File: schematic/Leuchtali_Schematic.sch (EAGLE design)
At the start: 34 parts, among them IC1 LM1458D, IC2 LM1458D, IC3 LM1458D, IC4 LT1618EMS#PBF

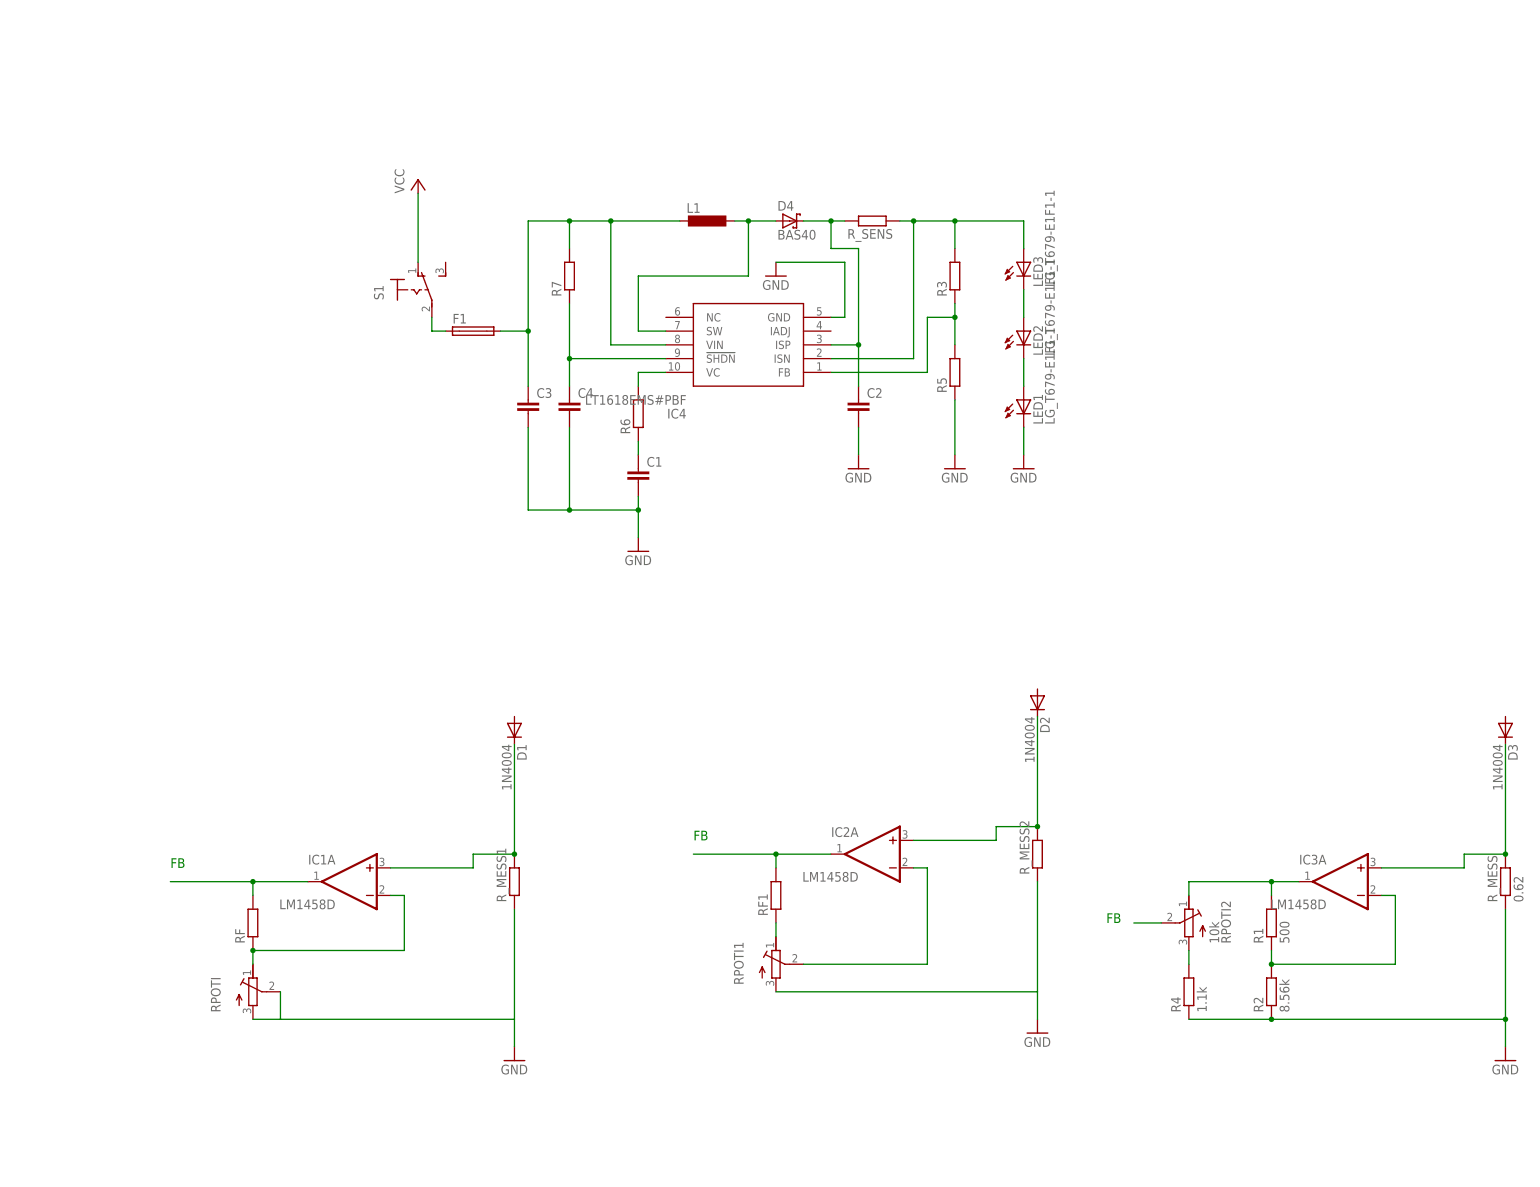
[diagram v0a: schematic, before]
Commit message: Removed old ideas from the schematic
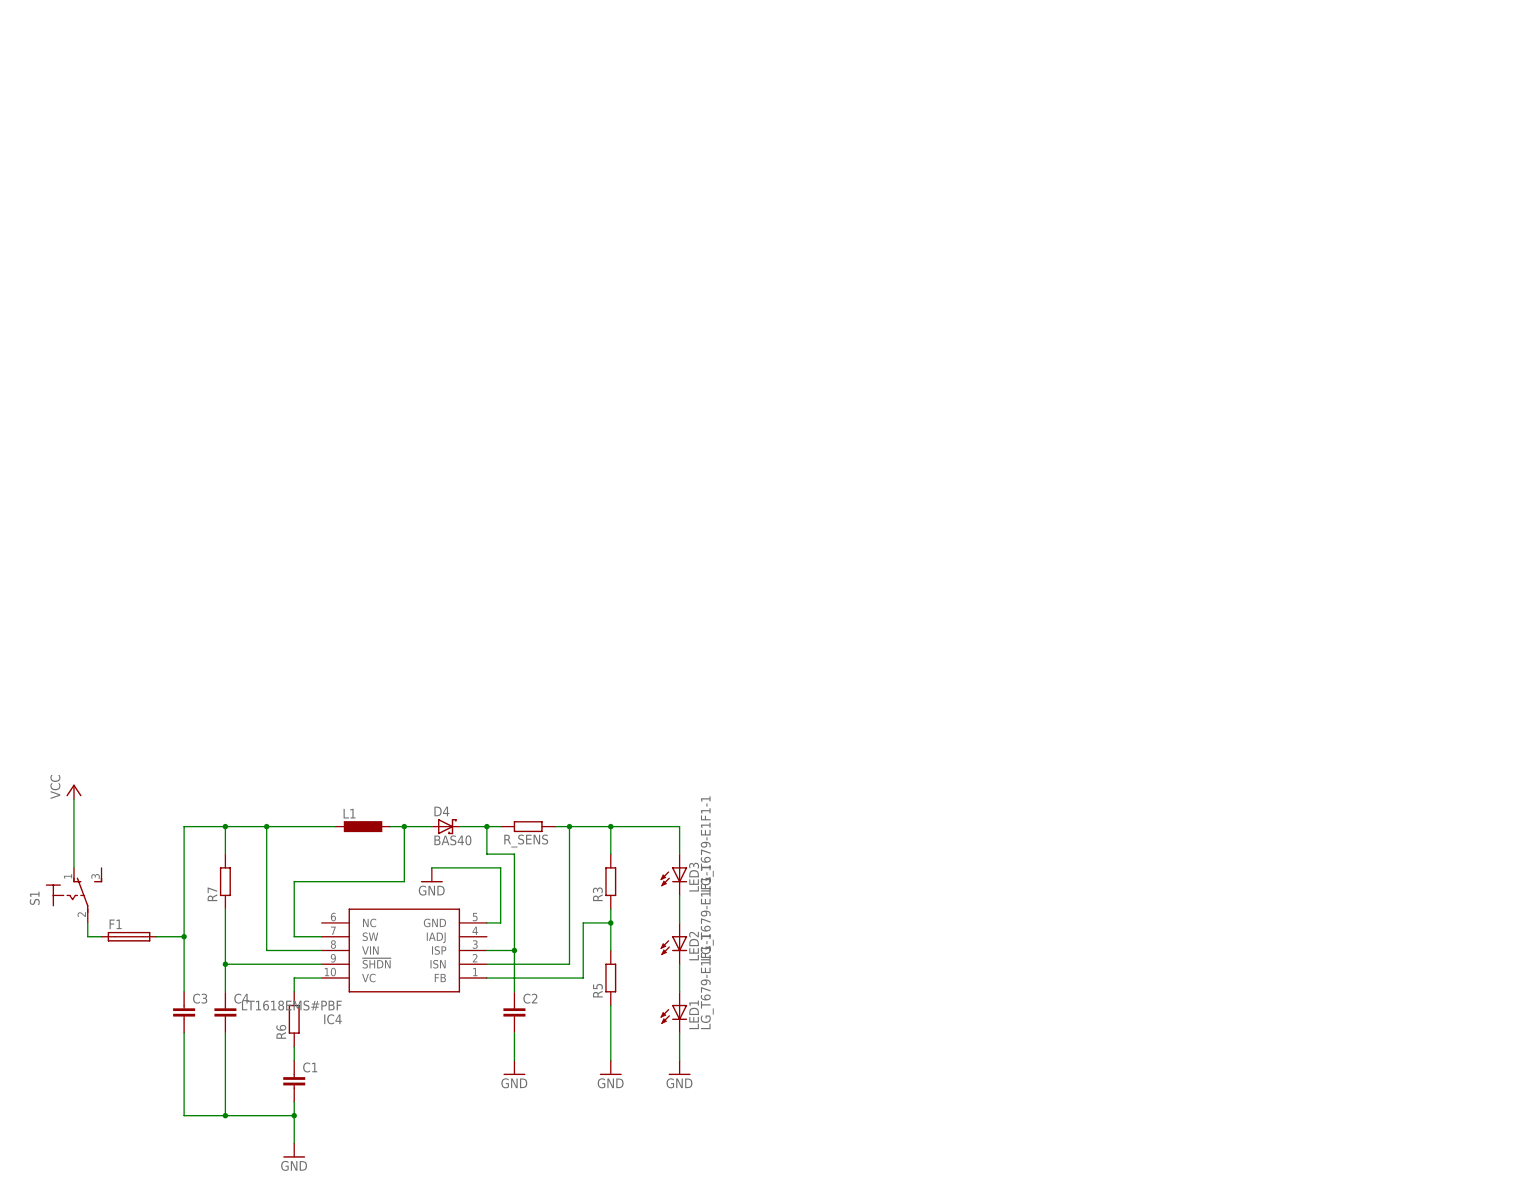
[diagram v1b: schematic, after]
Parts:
- removed D1, D2, D3: 1N4004, diode:1N4004
- removed IC1, IC2, IC3: LM1458D, linear:LM1458D
- removed R1: 500, rcl:R-EU_0204/2V
- removed R2: 8.56k, rcl:R-EU_0204/2V
- removed R4: 1.1k, rcl:R-EU_0204/2V
- removed RF, RF1: (no value), rcl:R-EU_0204/2V
- removed RPOTI, RPOTI1: (no value), rcl:R-TRIMMT93XA
- removed RPOTI2: 10k, rcl:R-TRIMMT93XA
- removed R_MESS: 0.62, rcl:R-EU_0617/22
- removed R_MESS1, R_MESS2: (no value), rcl:R-EU_0617/22
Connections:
- removed net N$1: D1.C, IC1A.+IN, R_MESS1.2
- removed net N$10: IC3A.-IN, R1.1, R2.2
- removed net N$11: R4.2, RPOTI2.A
- removed net N$12: RPOTI2.S
- removed net N$2: D2.C, IC2A.+IN, R_MESS2.2
- removed net N$3: IC1A.OUT, RF.2
- removed net N$4: IC2A.OUT, RF1.2
- removed net N$5: IC1A.-IN, RF.1, RPOTI.E
- removed net N$6: IC2A.-IN, RPOTI1.S
- removed net N$7: RF1.1, RPOTI1.E
- removed net N$8: D3.C, IC3A.+IN, R_MESS.2
- removed net N$9: IC3A.OUT, R1.2, RPOTI2.E
- net GND: no longer R2.1, R4.1, RPOTI.A, RPOTI.S, RPOTI1.A, R_MESS.1, R_MESS1.1, R_MESS2.1
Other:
- note removed: "FB"
- moved on the sheet: C1, C2, C3, C4, D4, F1, IC4, L1, LED1, LED2, LED3, R3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

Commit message: Continued working on the schematic
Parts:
- added C10: 0.33uF, rcl:C-EU025-024X044
- added C11, C12: (no value), rcl:C-EU025-024X044
- added C13, C17, C5: 10n, rcl:C-EUC0805
- added C14, C15, C18, C19, C6, C7: 4.7uF 25V, rcl:C-EUC0805
- added C16, C20, C8: 100nF, rcl:C-EUC0805
- added C9: 0.1uF, rcl:C-EU025-024X044
- added D1, D2, D3: BAS40, diode:BAS40
- added IC1: (no value), v-reg:78LXX
- added IC2, IC3, IC5: LT1618EMS#PBF, LT1618EMS:LT1618EMS#PBF
- added L2, L3, L4: 4.1uH 2A, rcl:L-EU0204/5
- added LED10, LED11, LED12, LED4, LED5, LED6, LED7, LED8, LED9: LG_T679-E1F1-1, led:LG_T679-E1F1-1
- added R1, R11: (no value), rcl:POTENTIOMETER_PT-10
- added R10, R16, R20: 15k, rcl:R-EU_R0805
- added R12, R2: (no value), rcl:R-EU_R0805
- added R13, R17, R4: 1.263k, rcl:R-EU_R0805
- added R14, R18, R8: 22.737k, rcl:R-EU_R0805
- added R15, R19, R9: 2k, rcl:R-EU_R0805
- added R_SENS1, R_SENS2, R_SENS3: 0.1, rcl:R-EU_R0805
- C1: value (none) -> 10n
- C2, C3: value (none) -> 4.7uF 25V
- C4: value (none) -> 100nF
- L1: value (none) -> 4.1uH 2A
- R3: value (none) -> 1.263k
- R5: value (none) -> 22.737k
- R6: value (none) -> 2k
- R7: value (none) -> 15k
- R_SENS: value (none) -> 0.1
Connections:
- new net IADJ_RED: C11.1, IC3.IADJ, IC4.IADJ, R1.3
- new net IADJ_WITHE: C12.1, IC2.IADJ, IC5.IADJ, R11.3
- new net N$1: R11.2, R12.1
- new net N$10: IC2.FB, R4.1, R8.2
- new net N$11: IC2.VC, R9.2
- new net N$12: C5.1, R9.1
- new net N$2: LED7.A, LED8.C
- new net N$23: C8.1, IC2.!SHDN, R10.1
- new net N$25: C14.1, D2.C, IC3.ISP, R_SENS2.2
- new net N$26: IC3.ISN, LED9.A, R13.2, R_SENS2.1
- new net N$27: IC3.FB, R13.1, R14.2
- new net N$28: IC3.VC, R15.2
- new net N$29: C13.1, R15.1
- new net N$3: R1.2, R2.1
- new net N$30: C16.1, IC3.!SHDN, R16.1
- new net N$31: LED10.A, LED11.C
- new net N$32: LED11.A, LED12.C
- new net N$33: D3.A, IC5.SW, L4.1
- new net N$34: C18.1, D3.C, IC5.ISP, R_SENS3.2
- new net N$35: IC5.ISN, LED12.A, R17.2, R_SENS3.1
- new net N$36: IC5.FB, R17.1, R18.2
- new net N$37: IC5.VC, R19.2
- new net N$38: C17.1, R19.1
- new net N$39: C20.1, IC5.!SHDN, R20.1
- new net N$4: LED8.A, LED9.C
- new net N$5: LED4.A, LED5.C
- new net N$6: LED5.A, LED6.C
- new net N$7: D1.A, IC2.SW, L2.1
- new net N$8: C6.1, D1.C, IC2.ISP, R_SENS1.2
- new net N$9: IC2.ISN, LED6.A, R4.2, R_SENS1.1
- new net VCC_33: C9.1, IC1.OUT, R12.2, R2.2
- new net VCC_FUSED: C10.1, C15.1, C19.1, C3.1, C7.1, F1.2, IC1.IN, IC2.VIN, IC3.VIN, IC4.VIN, IC5.VIN, L1.2, L2.2, L3.2, L4.2, R10.2, R16.2, R20.2, R7.2
- net GND: now also C10.2, C11.2, C12.2, C13.2, C14.2, C15.2, C16.2, C17.2, C18.2, C19.2, C20.2, C5.2, C6.2, C7.2, C8.2, C9.2, IC1.GND, IC2.GND, IC3.GND, IC5.GND, LED10.C, LED4.C, LED7.C, R1.1, R11.1, R14.1, R18.1, R8.1
- net N$22: now also D2.A, IC3.SW, L3.1; no longer C3.1, F1.2, IC4.VIN, L1.2, R7.2
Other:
- moved on the sheet: C1, C2, C3, C4, D4, F1, IC4, L1, LED1, LED2, LED3, R3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
